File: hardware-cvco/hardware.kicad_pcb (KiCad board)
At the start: 4 copper layers, 99 x 75 mm, 167 parts, among them J1 SMA, J2 SMA, J3 SMA, J4 SMA, J5 SMA, J6 SMA, J7 SMA, J8 Pickit 2, J9 DC, Q1 AOD403, Q2 MBT2222, SW1 On/Off, U1 74LS07, U10 TPS61046, U11 BQ21040, U12 LM324, U13 LM317DCYR, U14 LM386, U2 NLB-310-T1, U3 NLB-310-T1, U4 NLB-310-T1, U5 NLB-310-T1, U6 PIC12F675-ISN, U7 NLB-310-T1, U8 NLB-310-T1, U9 NLB-310-T1, Y1 CVCO55CW-0100-0200, Y2 CVCO55CW-0200-0500, Y3 CV55CW500-1000, Y4 CVCO55CW-1000-2000, Y5 CV55BE1600-3200, Y6 CVCO55CC-3180-3710, Y7 CVCO55CW-3500-4500

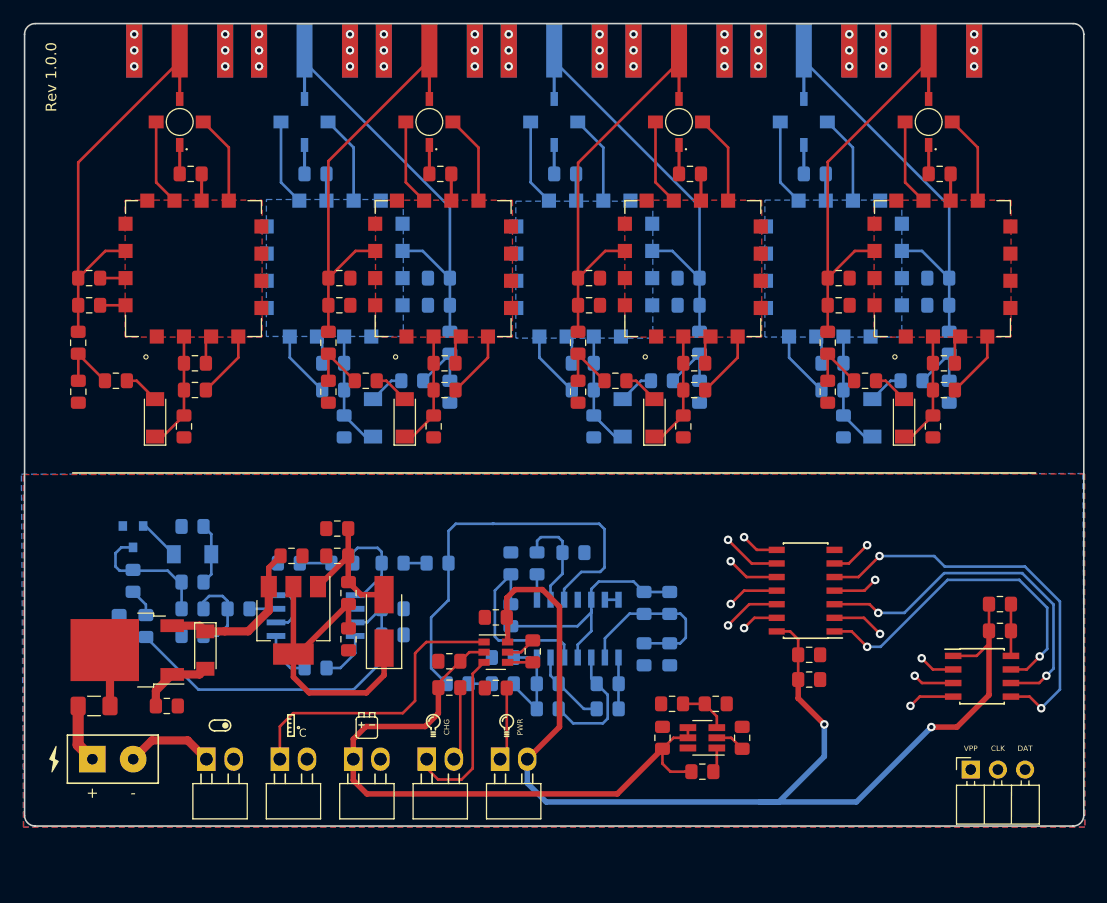
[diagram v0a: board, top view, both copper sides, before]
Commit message: Updated RF section - CVCO.
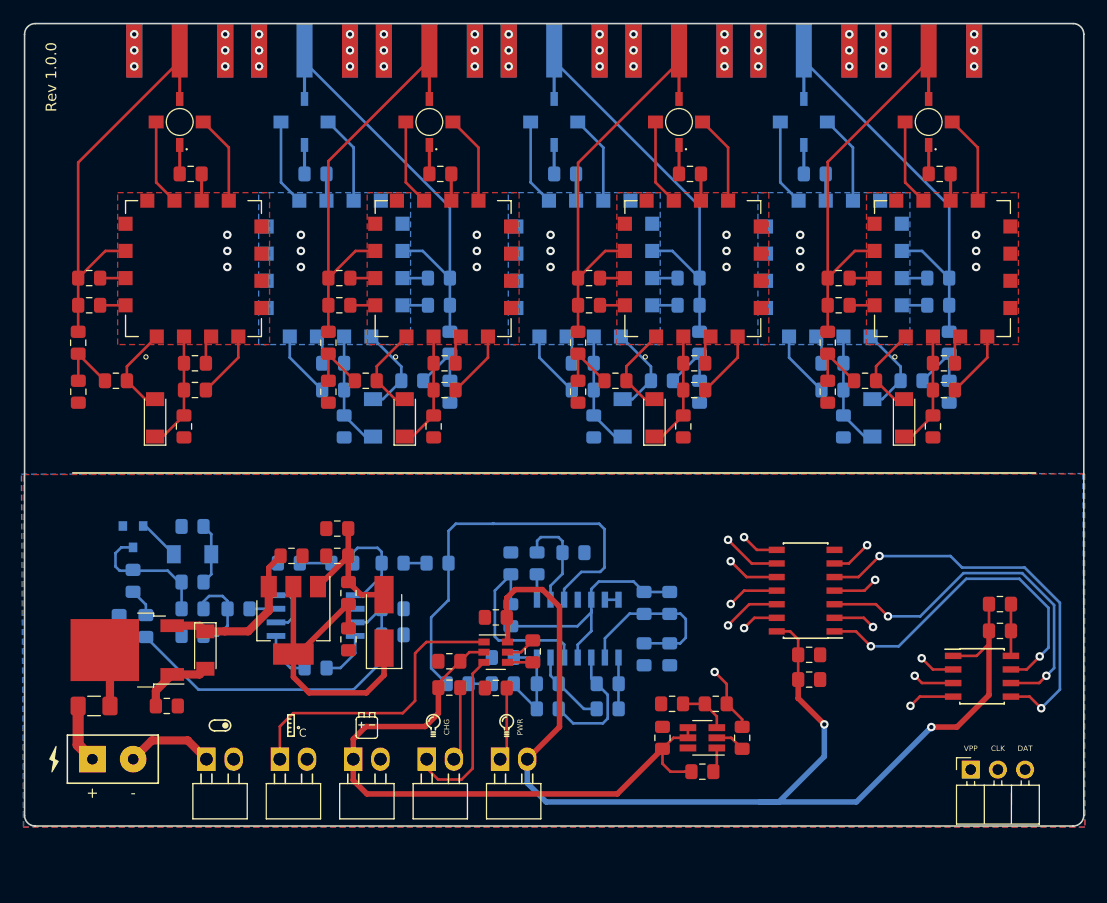
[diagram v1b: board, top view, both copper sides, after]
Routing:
- net GND: track 221.3 -> 286.5 mm, vias 42 -> 63
- net Boost: track 52.5 -> 57.8 mm, vias 6 -> 7

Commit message: Buffer routing - CVCO.
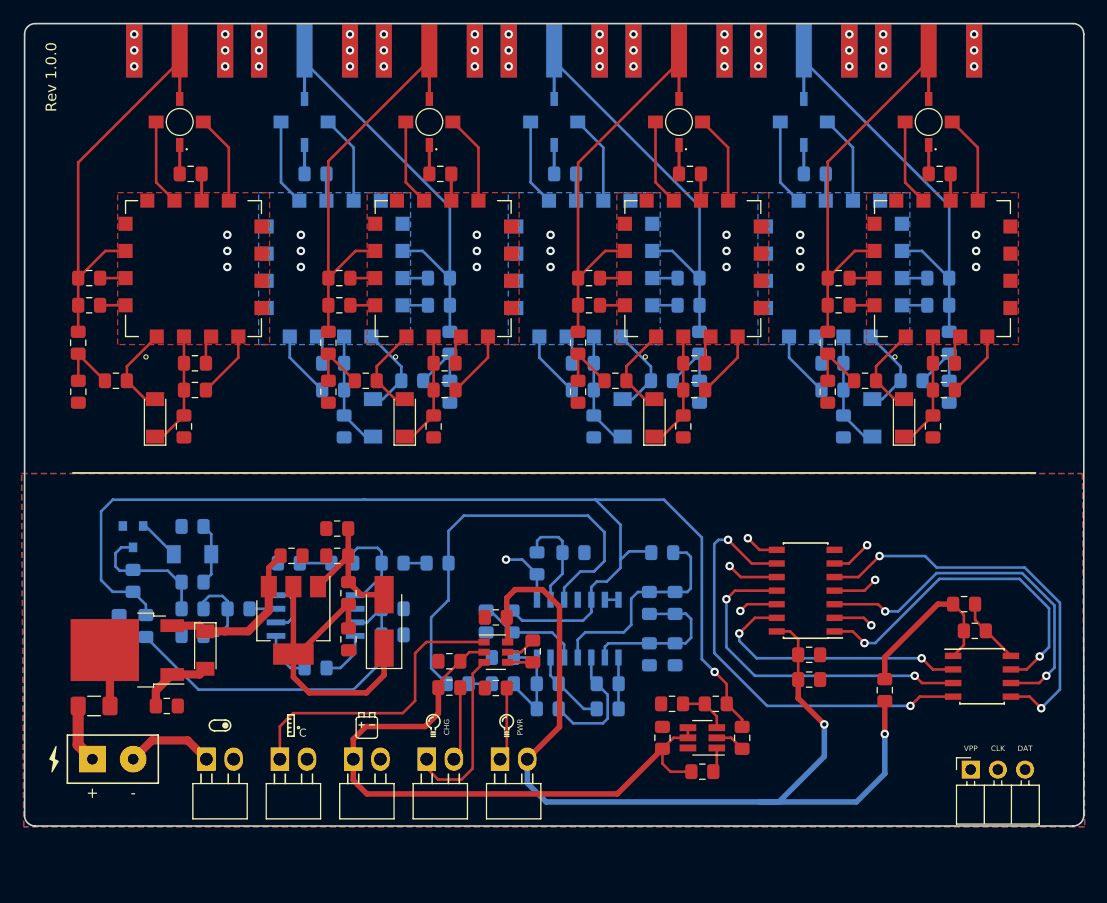
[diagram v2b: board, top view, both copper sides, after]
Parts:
- added R55: 150, Resistor_SMD:R_0805_2012Metric_Pad1.15x1.40mm_HandSolder, F.Cu at (145.9, 114.3)
- added R56: 480, Resistor_SMD:R_0805_2012Metric_Pad1.15x1.40mm_HandSolder, B.Cu at (125.1, 101.5)
- F1: value 2.5A Fast -> 1.5A Fast
- moved R52 5.90 mm to (108.6, 107.9), turned to 90 degrees
- moved C25 3.35 mm to (153.3, 106.3)
- moved C26 2.35 mm to (154.3, 108.8)
- moved R51 0.60 mm to (111.1, 107.9), turned to 90 degrees
- moved C49 0.50 mm to (123.9, 106.2)
- moved C53 0.50 mm to (123.9, 111.0)
- moved R38 0.50 mm to (126.3, 106.2)
- moved R46 0.50 mm to (126.3, 111.0)
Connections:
- C25 pad 1: VDD -> Net-(C25-Pad1)
- C26 pad 1: VDD -> Net-(C25-Pad1)
- C49 pad 1: Boost -> Net-(C49-Pad1)
- R38 pad 2: Boost -> Net-(C49-Pad1)
- U12 pad 4: Boost -> Net-(C49-Pad1)
- U6 pad 1: VDD -> Net-(C25-Pad1)
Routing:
- net Boost: track 57.8 -> 137.7 mm
- net GP3: track 20.1 -> 51.1 mm
- net GP4: track 8.69 -> 32.1 mm
- net Net-(C49-Pad1): track 0.00 -> 20.4 mm
- net VDD: track 111.3 -> 91.8 mm
- net GP5: track 6.82 -> 25.9 mm
- net Net-(C25-Pad1): track 0.00 -> 16.2 mm
- net Net-(R51-Pad1): track 17.2 -> 9.82 mm
- net Tuner: track 2.38 -> 5.85 mm, vias 0 -> 1
- net GND: track 286.5 -> 287.9 mm
- net VGND: track 16.4 -> 15.2 mm
- net GP0: track 46.0 -> 46.7 mm

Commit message: RF Section Buffer routing - CVCO.
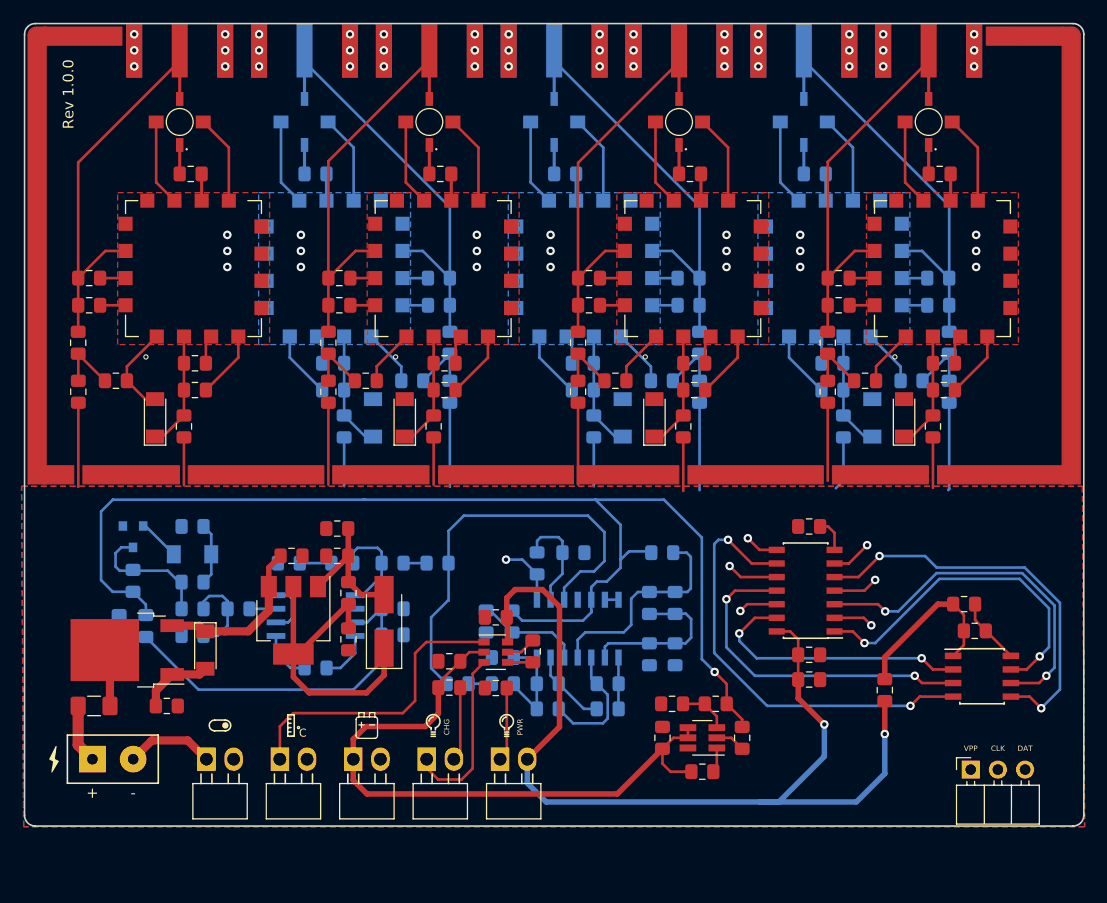
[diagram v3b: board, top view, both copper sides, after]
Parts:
- added R57: 100, Resistor_SMD:R_0805_2012Metric_Pad1.15x1.40mm_HandSolder, F.Cu at (138.8, 99.0)
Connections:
- C16 pad 2: GND -> INV0
- C17 pad 2: GND -> INV0
- C18 pad 2: GND -> INV1
- C19 pad 2: GND -> INV1
- C20 pad 2: GND -> INV2
- C21 pad 2: GND -> INV2
- C27 pad 2: GND -> INV3
- C28 pad 2: GND -> INV3
- C29 pad 2: GND -> INV4
- C3 pad 2: GND -> INV0
- C30 pad 2: GND -> INV4
- C31 pad 2: GND -> INV5
- C32 pad 2: GND -> INV5
- C37 pad 2: GND -> INV3
- C38 pad 2: GND -> INV3
- C39 pad 2: GND -> INV4
- C4 pad 2: GND -> INV0
- C40 pad 2: GND -> INV4
- C41 pad 2: GND -> INV5
- C42 pad 2: GND -> INV5
- C5 pad 2: GND -> INV1
- C6 pad 2: GND -> INV1
- C7 pad 2: GND -> Net-(C7-Pad2)
- C8 pad 2: GND -> Net-(C7-Pad2)
- J2 pad 2: GND -> INV0
- J3 pad 2: GND -> INV1
- J4 pad 2: GND -> INV2
- J5 pad 2: GND -> INV3
- J6 pad 2: GND -> INV4
- J7 pad 2: GND -> INV5
- R10 pad 2: GND -> INV0
- R11 pad 2: GND -> INV1
- R12 pad 2: GND -> INV2
- R25 pad 2: GND -> INV3
- R26 pad 2: GND -> INV4
- R27 pad 2: GND -> INV5
- U1 pad 10: Boost -> INV4
- U1 pad 12: Boost -> INV5
- U1 pad 2: Boost -> INV0
- U1 pad 4: Boost -> INV1
- U1 pad 6: Boost -> INV2
- U1 pad 7: GND -> Net-(R57-Pad1)
- U1 pad 8: Boost -> INV3
- U3 pad 2: GND -> INV0
- U3 pad 4: GND -> INV0
- U4 pad 2: GND -> INV1
- U4 pad 4: GND -> INV1
- U5 pad 2: GND -> INV2
- U5 pad 4: GND -> INV2
- U7 pad 2: GND -> INV3
- U7 pad 4: GND -> INV3
- U8 pad 2: GND -> INV4
- U8 pad 4: GND -> INV4
- U9 pad 2: GND -> INV5
- U9 pad 4: GND -> INV5
- Y2 pad 1: GND -> INV0
- Y2 pad 11: GND -> INV0
- Y2 pad 12: GND -> INV0
- Y2 pad 13: GND -> INV0
- Y2 pad 15: GND -> INV0
- Y2 pad 16: GND -> INV0
- Y2 pad 3: GND -> INV0
- Y2 pad 4: GND -> INV0
- Y2 pad 5: GND -> INV0
- Y2 pad 6: GND -> INV0
- Y2 pad 7: GND -> INV0
- Y2 pad 8: GND -> INV0
- Y2 pad 9: GND -> INV0
- Y3 pad 1: GND -> INV1
- Y3 pad 11: GND -> INV1
- Y3 pad 12: GND -> INV1
- Y3 pad 13: GND -> INV1
- Y3 pad 15: GND -> INV1
- Y3 pad 16: GND -> INV1
- Y3 pad 3: GND -> INV1
- Y3 pad 4: GND -> INV1
- Y3 pad 5: GND -> INV1
- Y3 pad 6: GND -> INV1
- Y3 pad 7: GND -> INV1
- Y3 pad 8: GND -> INV1
- Y3 pad 9: GND -> INV1
- Y4 pad 1: GND -> INV2
- Y4 pad 11: GND -> INV2
- Y4 pad 12: GND -> INV2
- Y4 pad 13: GND -> INV2
- Y4 pad 15: GND -> INV2
- Y4 pad 16: GND -> INV2
- Y4 pad 3: GND -> INV2
- Y4 pad 4: GND -> INV2
- Y4 pad 5: GND -> INV2
- Y4 pad 6: GND -> INV2
- Y4 pad 7: GND -> INV2
- Y4 pad 8: GND -> INV2
- Y4 pad 9: GND -> INV2
- Y5 pad 1: GND -> INV3
- Y5 pad 11: GND -> INV3
- Y5 pad 12: GND -> INV3
- Y5 pad 13: GND -> INV3
- Y5 pad 15: GND -> INV3
- Y5 pad 16: GND -> INV3
- Y5 pad 3: GND -> INV3
- Y5 pad 4: GND -> INV3
- Y5 pad 5: GND -> INV3
- Y5 pad 6: GND -> INV3
- Y5 pad 7: GND -> INV3
- Y5 pad 8: GND -> INV3
- Y5 pad 9: GND -> INV3
- Y6 pad 1: GND -> INV4
- Y6 pad 11: GND -> INV4
- Y6 pad 12: GND -> INV4
- Y6 pad 13: GND -> INV4
- Y6 pad 15: GND -> INV4
- Y6 pad 16: GND -> INV4
- Y6 pad 3: GND -> INV4
- Y6 pad 4: GND -> INV4
- Y6 pad 5: GND -> INV4
- Y6 pad 6: GND -> INV4
- Y6 pad 7: GND -> INV4
- Y6 pad 8: GND -> INV4
- Y6 pad 9: GND -> INV4
- Y7 pad 1: GND -> INV5
- Y7 pad 11: GND -> INV5
- Y7 pad 12: GND -> INV5
- Y7 pad 13: GND -> INV5
- Y7 pad 15: GND -> INV5
- Y7 pad 16: GND -> INV5
- Y7 pad 3: GND -> INV5
- Y7 pad 4: GND -> INV5
- Y7 pad 5: GND -> INV5
- Y7 pad 6: GND -> INV5
- Y7 pad 7: GND -> INV5
- Y7 pad 8: GND -> INV5
- Y7 pad 9: GND -> INV5
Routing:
- net GND: track 287.9 -> 60.4 mm, vias 63 -> 9
- net INV0: track 0.00 -> 155.0 mm, vias 0 -> 10
- net INV5: track 0.00 -> 151.5 mm, vias 0 -> 10
- net INV3: track 0.00 -> 150.0 mm, vias 0 -> 10
- net INV1: track 0.00 -> 131.1 mm, vias 0 -> 10
- net INV4: track 0.00 -> 127.7 mm, vias 0 -> 10
- net INV2: track 0.00 -> 115.5 mm, vias 0 -> 10
- net Tuner: track 5.85 -> 38.7 mm
- net Boost: track 137.7 -> 169.1 mm, vias 7 -> 1
- net Net-(R57-Pad1): track 0.00 -> 3.18 mm

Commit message: RF shield - CVCO.
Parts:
- turned D1 to 270 degrees
- turned D2 to 270 degrees
- turned D3 to 270 degrees
- turned D4 to 270 degrees
- turned D5 to 270 degrees
- turned D6 to 270 degrees
- turned D7 to 270 degrees
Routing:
- net GND: track 60.4 -> 296.3 mm, vias 9 -> 142
- net Boost: track 169.1 -> 170.4 mm
- net Tuner: track 38.7 -> 39.4 mm

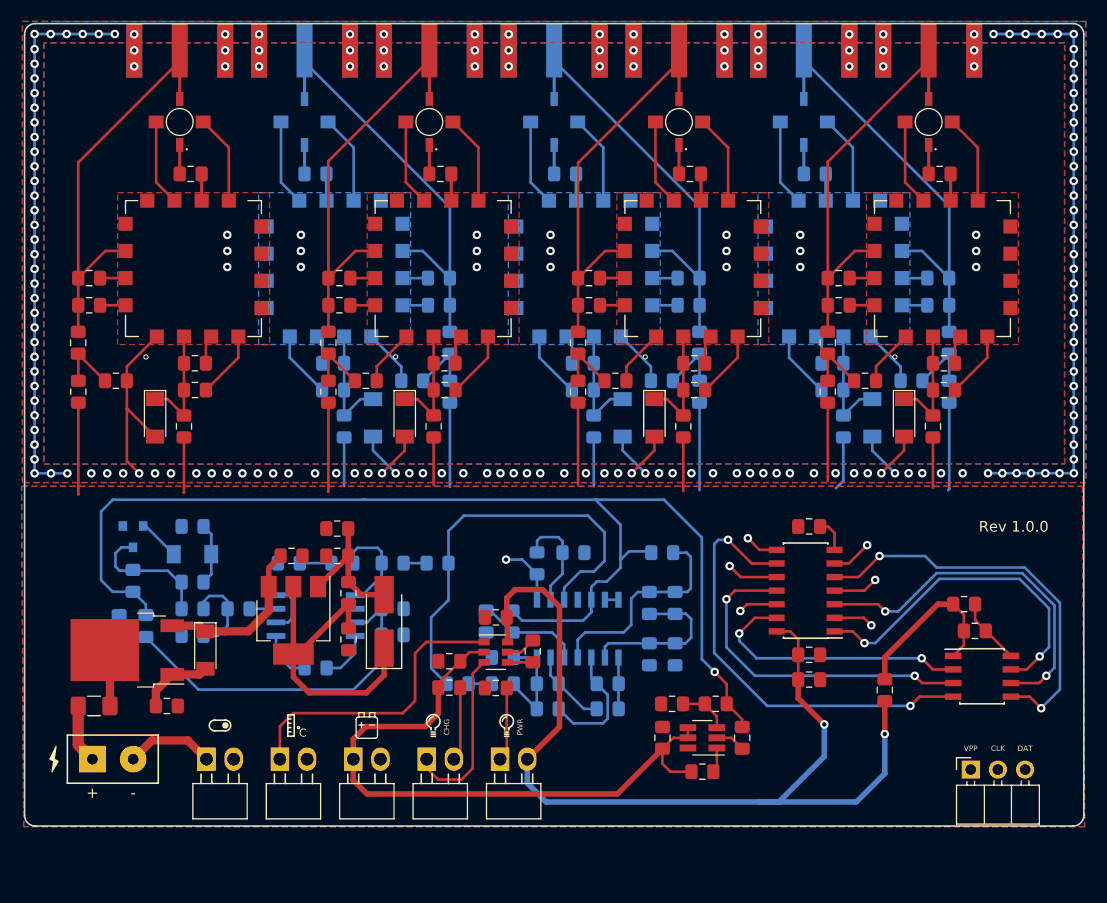
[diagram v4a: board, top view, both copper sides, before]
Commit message: Redone RF shield - CVCO.
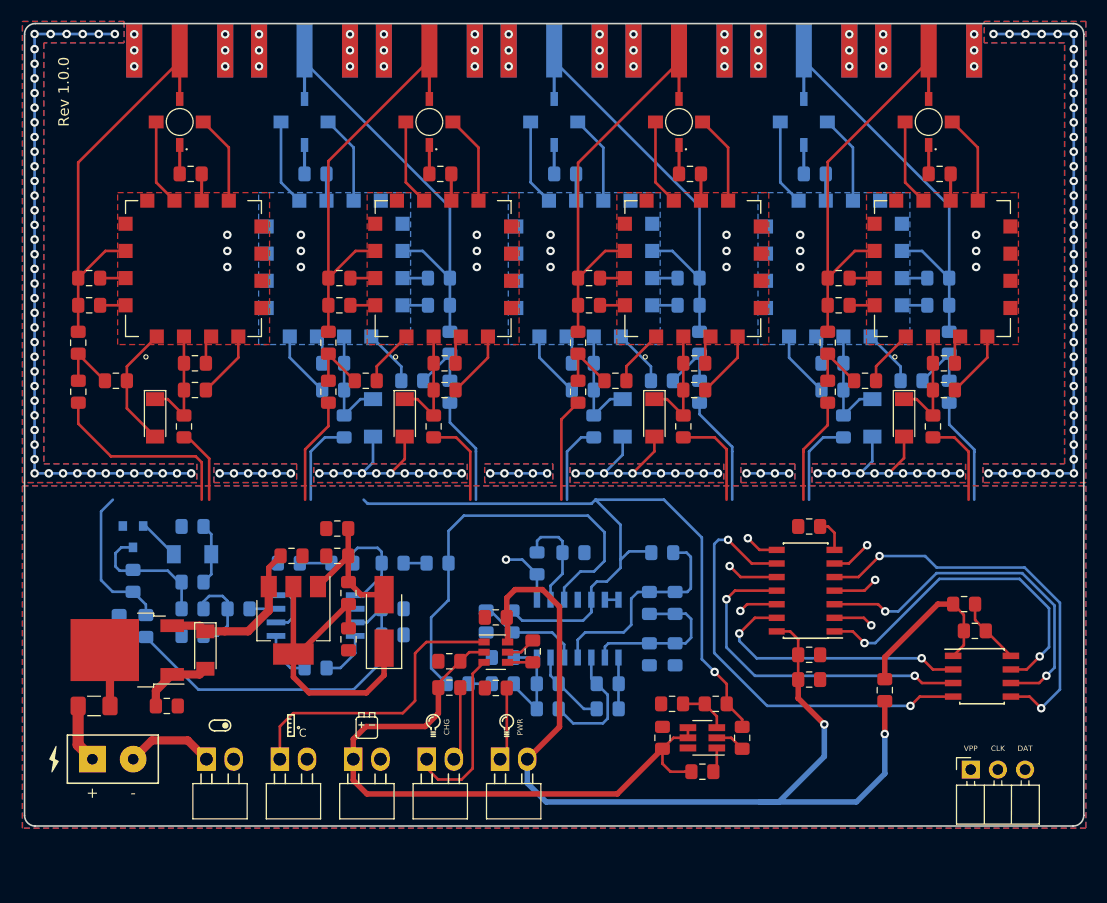
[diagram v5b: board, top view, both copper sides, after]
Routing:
- net GND: track 296.3 -> 269.5 mm, vias 142 -> 146
- net Tuner: track 39.4 -> 62.9 mm
- net INV0: track 155.0 -> 133.4 mm
- net INV2: track 115.5 -> 117.6 mm
- net INV5: track 151.5 -> 153.3 mm
- net INV3: track 150.0 -> 148.4 mm
- net INV4: track 127.7 -> 129.3 mm
- net Boost: track 170.4 -> 169.7 mm

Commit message: Finalized CVCO variant.
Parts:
- moved BT1 5.00 mm to (96.2, 125.8)
- moved C13 5.00 mm to (110.2, 118.7)
- moved C22 5.00 mm to (99.9, 107.4)
- moved C23 5.00 mm to (138.8, 116.0)
- moved C24 5.00 mm to (138.8, 118.3)
- moved C25 5.00 mm to (153.3, 111.3)
- moved C26 5.00 mm to (154.3, 113.8)
- moved C36 5.00 mm to (132.6, 123.8)
- moved C43 5.00 mm to (125.1, 123.8)
- moved C44 5.00 mm to (114.4, 118.7)
- moved C45 5.00 mm to (105.2, 116.6)
- moved C46 5.00 mm to (109.5, 112.5)
- moved C47 5.00 mm to (99.9, 111.7)
- moved C48 5.00 mm to (99.9, 114.1)
- moved C49 5.00 mm to (123.9, 111.2)
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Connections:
- C7 pad 2: Net-(C7-Pad2) -> INV2
- C8 pad 2: Net-(C7-Pad2) -> INV2
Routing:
- net Boost: track 169.7 -> 329.9 mm, vias 1 -> 4
- net Tuner: track 62.9 -> 171.0 mm, vias 1 -> 5
- net INV0: track 133.4 -> 161.1 mm
- net INV2: track 117.6 -> 123.4 mm
- net INV4: track 129.3 -> 134.0 mm
- net INV3: track 148.4 -> 153.1 mm
- net GND: track 269.5 -> 264.8 mm
- net Net-(R17-Pad1): track 40.0 -> 37.6 mm
- net INV5: track 153.3 -> 154.9 mm
- net INV1: track 131.4 -> 133.0 mm
- added copper zone on F.Cu, net INV0
- added copper zone on F.Cu, net INV1
- added copper zone on F.Cu, net INV2
- added copper zone on B.Cu, net INV3
- added copper zone on B.Cu, net INV4
- added copper zone on B.Cu, net INV5
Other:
- board size 99 x 75 mm -> 99 x 80 mm

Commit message: BOM & Gerber files - CVCO.
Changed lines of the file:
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@@
     (visible_elements FFFFFF7F)
     (pcbplotparams
-      (layerselection 0x01070_ffffffff)
+      (layerselection 0x010f0_ffffffff)
       (usegerberextensions false)
       (usegerberattributes false)
@@
   )
   (gr_arc (start 66.5 131) (end 65.5 131) (angle -90) (layer Edge.Cuts) (width 0.15))
-  (gr_text DAT (at 159.011666 124.75) (layer F.SilkS)
+  (gr_text DAT (at 156.471666 124.75) (layer F.SilkS)
     (effects (font (size 0.5 0.5) (thickness 0.1)))
   )
-  (gr_text CLK (at 156.471666 124.75) (layer F.SilkS)
+  (gr_text CLK (at 159.011666 124.75) (layer F.SilkS)
     (effects (font (size 0.5 0.5) (thickness 0.1)))
   )
